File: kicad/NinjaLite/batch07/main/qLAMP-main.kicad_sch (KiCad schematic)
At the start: 17 parts, among them J3 Conn_01x07_Male, J5 Conn_01x14_Male, J6 Conn_01x01_Male, J7 Conn_01x04_Male, Q3 Q_NMOS_GSD, Q5 Q_NMOS_GSD, U12 ESP32-­S3-­WROOM­-1

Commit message: sync
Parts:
- removed J5: Conn_01x14_Male, Pin_Headers:Pin_Header_Straight_1x14_Pitch2.54mm, symbol Connector:Conn_01x14_Male
- added J5, J8: Conn_01x07_Male, Pin_Headers:Pin_Header_Straight_1x07_Pitch2.54mm, symbol Connector:Conn_01x07_Male
- added J9: Conn_01x02_Pin, symbol Connector:Conn_01x02_Pin
- added R12: 100k, Resistor_SMD:R_0603_1608Metric, symbol Device:R
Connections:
- net 3V3D: now also J5.7 (Pin_7), J8.7 (Pin_7), R12.2
- net GND: now also J8.6 (Pin_6), J9.2 (Pin_2)
- net LCD_CS: now also J8.5 (Pin_5)
- net LCD_DC/RS: now also J8.3 (Pin_3)
- net LCD_RESET: now also J8.4 (Pin_4)
- net SD_CLK: now also J5.5 (Pin_5), J8.1 (Pin_1)
- net SD_MISO: now also J5.2 (Pin_2), J5.6 (Pin_6)
- net SD_MOSI: now also J5.3 (Pin_3), J8.2 (Pin_2)
- net TP_CS: now also J5.4 (Pin_4)
- net TP_IRQ: now also J5.1 (Pin_1)
- net at U12.27 (IO0): now also J9.1 (Pin_1), R12.1
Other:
- note added: "Don't pull-up IO46"
- note added: "IO0 has internal pull-up. Try without soldering R first. If it works, you can remove external pull-up circuit."

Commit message: wiring batch7
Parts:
- removed J6: Conn_01x01_Male, Pin_Headers:Pin_Header_Straight_1x01_Pitch1.27mm, symbol Connector:Conn_01x01_Male
- removed R23: 100k, Resistor_SMD:R_0603_1608Metric, symbol Device:R
- added J10: Conn_01x08_Pin, Connector_PinHeader_2.54mm:PinHeader_2x04_P2.54mm_Vertical, symbol Connector:Conn_01x08_Pin
- added J6: Conn_01x01_Pin, Connector_PinHeader_2.54mm:PinHeader_1x01_P2.54mm_Vertical, symbol Connector:Conn_01x01_Pin
- added SW1: TACTILE_4, Ninja:SW_TH_Tactile_alps_SKHHLPA010, symbol Ninja:TACTILE_4
- HLID1, HWELL1: footprint Ninja-qPCR:TB_SeeedOPL_320110028 -> Ninja:TB_SeeedOPL_320110028
- J5, J8: footprint Pin_Headers:Pin_Header_Straight_1x07_Pitch2.54mm -> Connector_PinHeader_2.54mm:PinHeader_1x07_P2.54mm_Vertical
- J7: footprint Pin_Headers:Pin_Header_Straight_1x04_Pitch2.54mm -> Connector_PinHeader_2.54mm:PinHeader_1x04_P2.54mm_Vertical
- J9: footprint (none) -> Connector_PinHeader_2.54mm:PinHeader_1x02_P2.54mm_Vertical
- Q3, Q5: footprint Ninja-qPCR:SOT95P240X112-3N -> Ninja:SOT95P240X112-3N
- U12: footprint Ninja-qPCR:ESP32-S3-WROOM-1 -> Ninja:ESP32-S3-WROOM-1
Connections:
- net SD_CD is gone; now on net LID_HEATER: U12.7 (IO7)
- net TACT2 is gone; now on net BOOTMODE: J3.1 (Pin_1)
- net 3V3D: now also J10.3 (Pin_3)
- net GND: now also J10.1 (Pin_1), J10.2 (Pin_2), SW1.3, SW1.4; no longer J9.2 (Pin_2)
- net I2C_SCL: now also U12.30 (IO37); no longer U12.14 (IO20)
- net I2C_SDA: now also U12.31 (IO38); no longer U12.17 (IO9)
- net LCD_CS: now also U12.16 (IO46); no longer U12.20 (IO12)
- net LCD_RESET: now also U12.17 (IO9); no longer U12.19 (IO11)
- net LED_BLANK: now also U12.28 (IO35); no longer U12.25 (IO48)
- net LED_LAT: now also U12.26 (IO45); no longer U12.13 (IO19)
- net LID_HEATER: no longer U12.11 (IO18)
- net MOSI: now also J5.3 (Pin_3), J8.2 (Pin_2), U12.23 (IO21); no longer U12.39 (IO1)
- net MUX_S0: now also U12.33 (IO40); no longer U12.28 (IO35)
- net MUX_S3: now also U12.34 (IO41); no longer U12.29 (IO36)
- net NAU_DRDY: now also U12.29 (IO36); no longer U12.6 (IO6)
- net SCLK: now also J5.5 (Pin_5), J8.1 (Pin_1), U12.21 (IO13); no longer U12.32 (IO39)
- net SD_CLK: now also U12.12 (IO8); no longer J5.5 (Pin_5), J8.1 (Pin_1), U12.23 (IO21)
- net SD_CS: now also U12.15 (IO3); no longer U12.24 (IO47)
- net SD_MISO: now also U12.13 (IO19); no longer J5.2 (Pin_2), J5.6 (Pin_6), U12.22 (IO14)
- net SD_MOSI: now also U12.14 (IO20); no longer J5.3 (Pin_3), J8.2 (Pin_2), U12.21 (IO13)
- net THERM_R_SWITCH: now also U12.32 (IO39); no longer U12.12 (IO8)
- net TP_CS: now also U12.24 (IO47)
- net TP_IRQ: now also U12.25 (IO48)
- net VIN_SENSE: now also U12.10 (IO17); no longer U12.8 (IO15)
- net WELL_HEATER: now also U12.8 (IO15); no longer U12.10 (IO17)
- net BOOTMODE: now reaches R12.1, U12.27 (IO0)
- net BOOTMODE: now also SW1.1, SW1.2; no longer J9.1 (Pin_1)
- net IO4: now reaches U12.4 (IO4)
- net IO4: now also J10.4 (Pin_4)
- net IO5: now reaches U12.5 (IO5)
- net IO5: now also J10.5 (Pin_5)
- net IO16: now reaches U12.9 (IO16)
- net IO16: now also J10.7 (Pin_7)
- new net IO1: J6.1 (Pin_1), U12.39 (IO1)
- new net IO11: J9.1 (Pin_1), U12.19 (IO11)
- new net IO12: J9.2 (Pin_2), U12.20 (IO12)
- new net IO18: J10.8 (Pin_8), U12.11 (IO18)
- new net IO6: J10.6 (Pin_6), U12.6 (IO6)
- new net MISO: J5.2 (Pin_2), J5.6 (Pin_6), U12.22 (IO14)
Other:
- moved on the sheet: J7

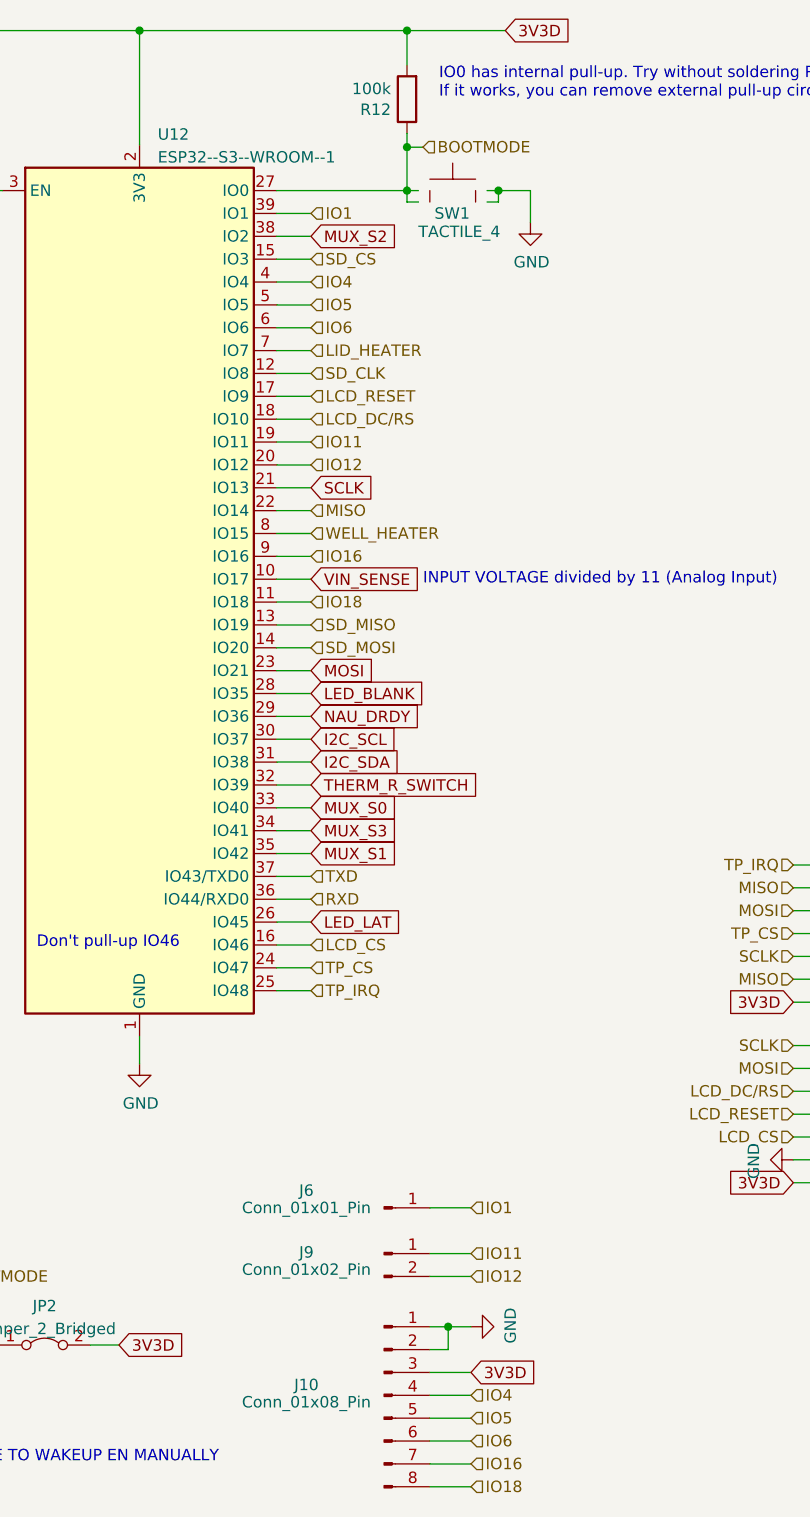
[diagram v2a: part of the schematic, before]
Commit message: wiring batch7 main
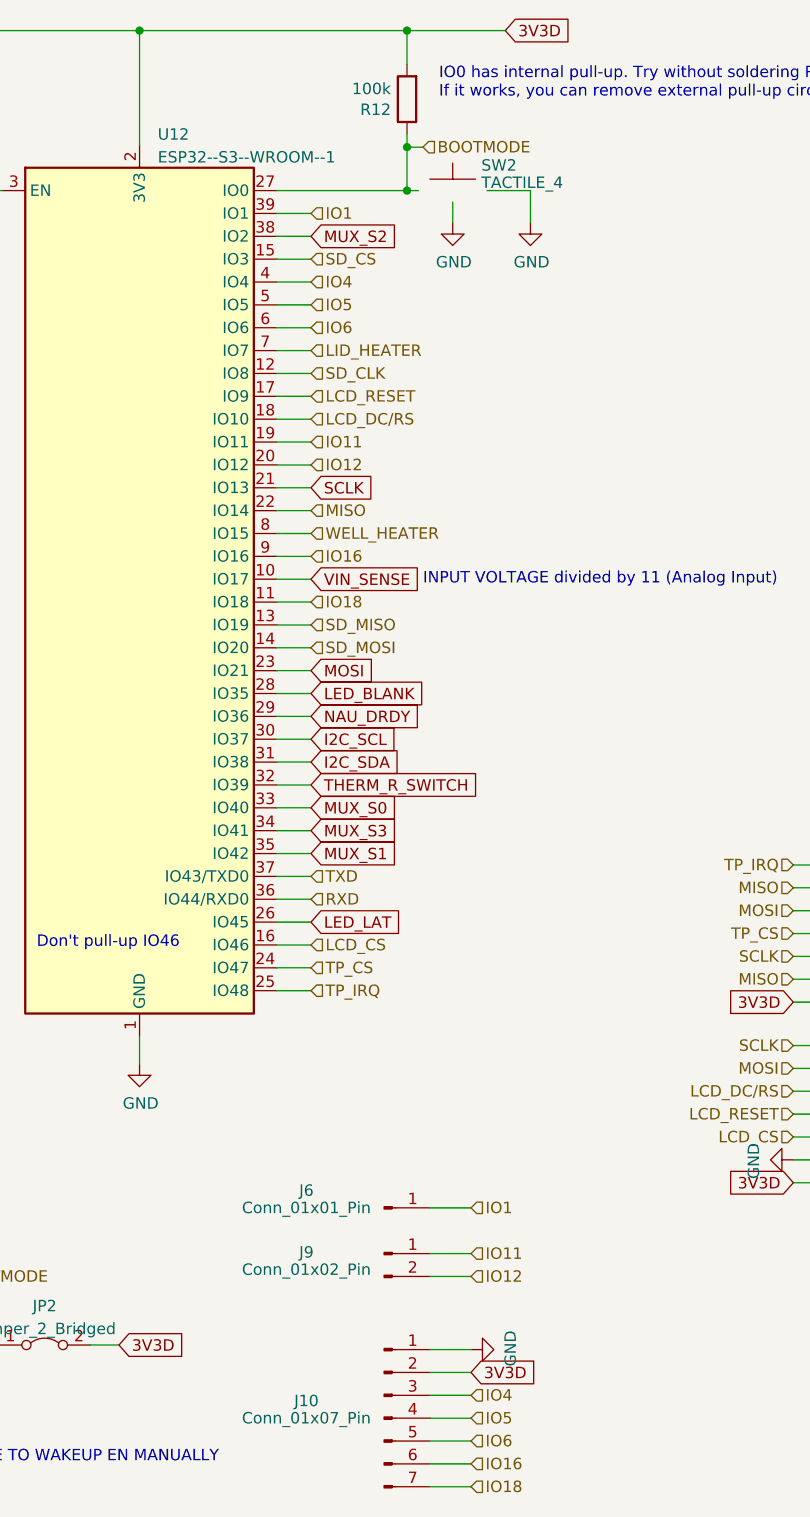
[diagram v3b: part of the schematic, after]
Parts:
- removed J10: Conn_01x08_Pin, Connector_PinHeader_2.54mm:PinHeader_2x04_P2.54mm_Vertical, symbol Connector:Conn_01x08_Pin
- removed SW1: TACTILE_4, Ninja:SW_TH_Tactile_alps_SKHHLPA010, symbol Ninja:TACTILE_4
- added J10: Conn_01x07_Pin, Connector_PinHeader_2.54mm:PinHeader_1x07_P2.54mm_Vertical, symbol Connector:Conn_01x07_Pin
- added SW2: TACTILE_4, Ninja:SW_TH_Tactile_alps_SKHHLPA010, symbol Ninja:TACTILE_SKHHLPA010
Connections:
- net 3V3D: now also J10.2 (Pin_2)
- net BOOTMODE: now also SW2.1
- net GND: now also J10.1 (Pin_1), SW2.2, SW2.GND
- net IO16: now also J10.6 (Pin_6)
- net IO18: now also J10.7 (Pin_7)
- net IO4: now also J10.3 (Pin_3)
- net IO5: now also J10.4 (Pin_4)
- net IO6: now also J10.5 (Pin_5)
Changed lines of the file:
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@@
   (junction (at 58.42 32.004) (diameter 0) (color 0 0 0 0)
   )
-  (junction (at 92.71 176.022) (diameter 0) (color 0 0 0 0)
-  )
   (junction (at 88.138 44.958) (diameter 0) (color 0 0 0 0)
   )
@@
   )
   (junction (at 88.138 32.004) (diameter 0) (color 0 0 0 0)
-  )
-  (junction (at 98.298 49.784) (diameter 0) (color 0 0 0 0)
   )
   (junction (at 88.138 49.784) (diameter 0) (color 0 0 0 0)
@@
     (stroke (width 0) (type default))
   )
-  (wire (pts (xy 89.408 51.054) (xy 88.138 51.054))
-    (stroke (width 0) (type default))
-  )
   (wire (pts (xy 73.66 120.904) (xy 77.47 120.904))
     (stroke (width 0) (type default))
@@
     (stroke (width 0) (type default))
   )
-  (wire (pts (xy 90.678 178.562) (xy 92.71 178.562))
+  (wire (pts (xy 90.678 178.562) (xy 95.25 178.562))
     (stroke (width 0) (type default))
   )
@@
     (stroke (width 0) (type default))
   )
-  (wire (pts (xy 92.71 176.022) (xy 95.25 176.022))
-    (stroke (width 0) (type default))
-  )
   (wire (pts (xy 30.734 172.974) (xy 36.449 172.974))
     (stroke (width 0) (type default))
@@
     (stroke (width 0) (type default))
   )
-  (wire (pts (xy 98.298 51.054) (xy 98.298 49.784))
-    (stroke (width 0) (type default))
-  )
   (wire (pts (xy 33.02 49.784) (xy 43.18 49.784))
     (stroke (width 0) (type default))
@@
     (stroke (width 0) (type default))
   )
-  (wire (pts (xy 98.298 49.784) (xy 101.854 49.784))
-    (stroke (width 0) (type default))
-  )
   (wire (pts (xy 194.056 72.39) (xy 194.056 74.93))
     (stroke (width 0) (type default))
@@
     (stroke (width 0) (type default))
   )
+  (wire (pts (xy 93.218 51.054) (xy 93.218 53.34))
+    (stroke (width 0) (type default))
+  )
   (wire (pts (xy 131.064 137.414) (xy 135.128 137.414))
     (stroke (width 0) (type default))
@@
     (stroke (width 0) (type default))
   )
-  (wire (pts (xy 92.71 178.562) (xy 92.71 176.022))
-    (stroke (width 0) (type default))
-  )
   (wire (pts (xy 33.02 49.784) (xy 33.02 52.324))
     (stroke (width 0) (type default))
@@
     (stroke (width 0) (type default))
   )
-  (wire (pts (xy 88.138 51.054) (xy 88.138 49.784))
-    (stroke (width 0) (type default))
-  )
   (wire (pts (xy 73.66 59.944) (xy 77.47 59.944))
     (stroke (width 0) (type default))
@@
     (stroke (width 0) (type default))
   )
-  (wire (pts (xy 90.678 176.022) (xy 92.71 176.022))
-    (stroke (width 0) (type default))
-  )
-  (wire (pts (xy 97.028 49.784) (xy 98.298 49.784))
+  (wire (pts (xy 97.028 49.784) (xy 101.854 49.784))
     (stroke (width 0) (type default))
   )
@@
   )
   (wire (pts (xy 187.706 35.052) (xy 194.056 35.052))
-    (stroke (width 0) (type default))
-  )
-  (wire (pts (xy 97.028 51.054) (xy 98.298 51.054))
     (stroke (width 0) (type default))
   )
@@
         (path "/86ad0555-08b3-4dde-9a3e-c1e5e29b6615"
           (reference "HLID1") (unit 1)
+        )
+      )
+    )
+  )
+  (symbol (lib_id "power:GND") (at 93.218 53.34 0) (unit 1)
+    (in_bom yes) (on_board yes) (dnp no)
+    (property "Reference" "#PWR03" (at 93.218 59.69 0)
+      (effects (font (size 1.27 1.27)) hide)
+    )
+    (property "Value" "GND" (at 93.345 57.7342 0)
+      (effects (font (size 1.27 1.27)))
+    )
+    (property "Footprint" "" (at 93.218 53.34 0)
+      (effects (font (size 1.27 1.27)) hide)
+    )
+    (property "Datasheet" "" (at 93.218 53.34 0)
+      (effects (font (size 1.27 1.27)) hide)
+    )
+    (pin "1")
+    (instances
+      (project "qLAMP-main"
+        (path "/86ad0555-08b3-4dde-9a3e-c1e5e29b6615"
+          (reference "#PWR03") (unit 1)
         )
       )
@@
     )
   )
-  (symbol (lib_id "Ninja:TACTILE_4") (at 93.218 49.784 0) (unit 1)
-    (in_bom yes) (on_board yes) (dnp no)
-    (property "Reference" "SW1" (at 91.186 52.324 0)
-      (effects (font (size 1.27 1.27)) (justify left))
-    )
-    (property "Value" "TACTILE_4" (at 89.408 54.356 0)
-      (effects (font (size 1.27 1.27)) (justify left))
-    )
-    (property "Footprint" "Ninja:SW_TH_Tactile_alps_SKHHLPA010" (at 93.218 44.704 0)
-      (effects (font (size 1.27 1.27)) hide)
-    )
-    (property "Datasheet" "http://www.apem.com/int/index.php?controller=attachment&id_attachment=488" (at 93.218 44.704 0)
-      (effects (font (size 1.27 1.27)) hide)
-    )
-    (pin "1")
-    (pin "2")
-    (pin "3")
-    (pin "4")
-    (instances
-      (project "qLAMP-main"
-        (path "/86ad0555-08b3-4dde-9a3e-c1e5e29b6615"
-          (reference "SW1") (unit 1)
-        )
-      )
-    )
-  )
   (symbol (lib_id "power:GND") (at 131.064 157.48 270) (unit 1)
     (in_bom yes) (on_board yes) (dnp no)
@@
         (path "/86ad0555-08b3-4dde-9a3e-c1e5e29b6615"
           (reference "#PWR0106") (unit 1)
-        )
-      )
-    )
-  )
-  (symbol (lib_id "Connector:Conn_01x08_Pin") (at 85.598 183.642 0) (unit 1)
-    (in_bom yes) (on_board yes) (dnp no)
-    (property "Reference" "J10" (at 76.962 182.483 0)
-      (effects (font (size 1.27 1.27)))
-    )
-    (property "Value" "Conn_01x08_Pin" (at 76.962 184.404 0)
-      (effects (font (size 1.27 1.27)))
-    )
-    (property "Footprint" "Connector_PinHeader_2.54mm:PinHeader_2x04_P2.54mm_Vertical" (at 85.598 183.642 0)
-      (effects (font (size 1.27 1.27)) hide)
-    )
-    (property "Datasheet" "~" (at 85.598 183.642 0)
-      (effects (font (size 1.27 1.27)) hide)
-    )
-    (pin "1")
-    (pin "2")
-    (pin "3")
-    (pin "4")
-    (pin "5")
-    (pin "6")
-    (pin "7")
-    (pin "8")
-    (instances
-      (project "qLAMP-main"
-        (path "/86ad0555-08b3-4dde-9a3e-c1e5e29b6615"
-          (reference "J10") (unit 1)
         )
       )
@@
         (path "/86ad0555-08b3-4dde-9a3e-c1e5e29b6615"
           (reference "J6") (unit 1)
+        )
+      )
+    )
+  )
+  (symbol (lib_id "Ninja:TACTILE_SKHHLPA010") (at 93.218 49.784 0) (unit 1)
+    (in_bom yes) (on_board yes) (dnp no) (fields_autoplaced)
+    (property "Reference" "SW2" (at 96.393 46.9813 0)
+      (effects (font (size 1.27 1.27)) (justify left))
+    )
+    (property "Value" "TACTILE_4" (at 96.393 48.9023 0)
+      (effects (font (size 1.27 1.27)) (justify left))
+    )
+    (property "Footprint" "Ninja:SW_TH_Tactile_alps_SKHHLPA010" (at 93.218 44.704 0)
+      (effects (font (size 1.27 1.27)) hide)
+    )
+    (property "Datasheet" "http://www.apem.com/int/index.php?controller=attachment&id_attachment=488" (at 93.218 44.704 0)
+      (effects (font (size 1.27 1.27)) hide)
+    )
+    (pin "1")
+    (pin "2")
+    (pin "GND")
+    (instances
+      (project "qLAMP-main"
+        (path "/86ad0555-08b3-4dde-9a3e-c1e5e29b6615"
+          (reference "SW2") (unit 1)
         )
       )
@@
     )
   )
-  (symbol (lib_id "power:GND") (at 95.25 176.022 90) (unit 1)
-    (in_bom yes) (on_board yes) (dnp no)
-    (property "Reference" "#PWR02" (at 101.6 176.022 0)
-      (effects (font (size 1.27 1.27)) hide)
-    )
-    (property "Value" "GND" (at 99.6442 175.895 0)
-      (effects (font (size 1.27 1.27)))
-    )
-    (property "Footprint" "" (at 95.25 176.022 0)
-      (effects (font (size 1.27 1.27)) hide)
-    )
-    (property "Datasheet" "" (at 95.25 176.022 0)
+  (symbol (lib_id "power:GND") (at 95.25 178.562 90) (unit 1)
+    (in_bom yes) (on_board yes) (dnp no)
+    (property "Reference" "#PWR02" (at 101.6 178.562 0)
+      (effects (font (size 1.27 1.27)) hide)
+    )
+    (property "Value" "GND" (at 99.6442 178.435 0)
+      (effects (font (size 1.27 1.27)))
+    )
+    (property "Footprint" "" (at 95.25 178.562 0)
+      (effects (font (size 1.27 1.27)) hide)
+    )
+    (property "Datasheet" "" (at 95.25 178.562 0)
       (effects (font (size 1.27 1.27)) hide)
     )
@@
         )
       )
+    )
+  )
+  (symbol (lib_id "Connector:Conn_01x07_Pin") (at 85.598 186.182 0) (unit 1)
+    (in_bom yes) (on_board yes) (dnp no)
+    (property "Reference" "J10" (at 76.962 184.261 0)
+      (effects (font (size 1.27 1.27)))
+    )
+    (property "Value" "Conn_01x07_Pin" (at 76.962 186.182 0)
+      (effects (font (size 1.27 1.27)))
+    )
+    (property "Footprint" "Connector_PinHeader_2.54mm:PinHeader_1x07_P2.54mm_Vertical" (at 85.598 186.182 0)
+      (effects (font (size 1.27 1.27)) hide)
+    )
+    (property "Datasheet" "~" (at 85.598 186.182 0)
+      (effects (font (size 1.27 1.27)) hide)
+    )
+    (pin "1")
+    (pin "2")
+    (pin "3")
+    (pin "4")
+    (pin "5")
+    (pin "6")
+    (pin "7")
+    (instances
+      (project "qLAMP-main"
+        (path "/86ad0555-08b3-4dde-9a3e-c1e5e29b6615"
+          (reference "J10") (unit 1)
+        )
+      )
